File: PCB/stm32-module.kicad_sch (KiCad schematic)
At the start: 26 parts, among them J1 Conn_01x30_Socket, J2 Conn_01x30_Socket, J3 TYPE-C_16PIN_2MD__073_

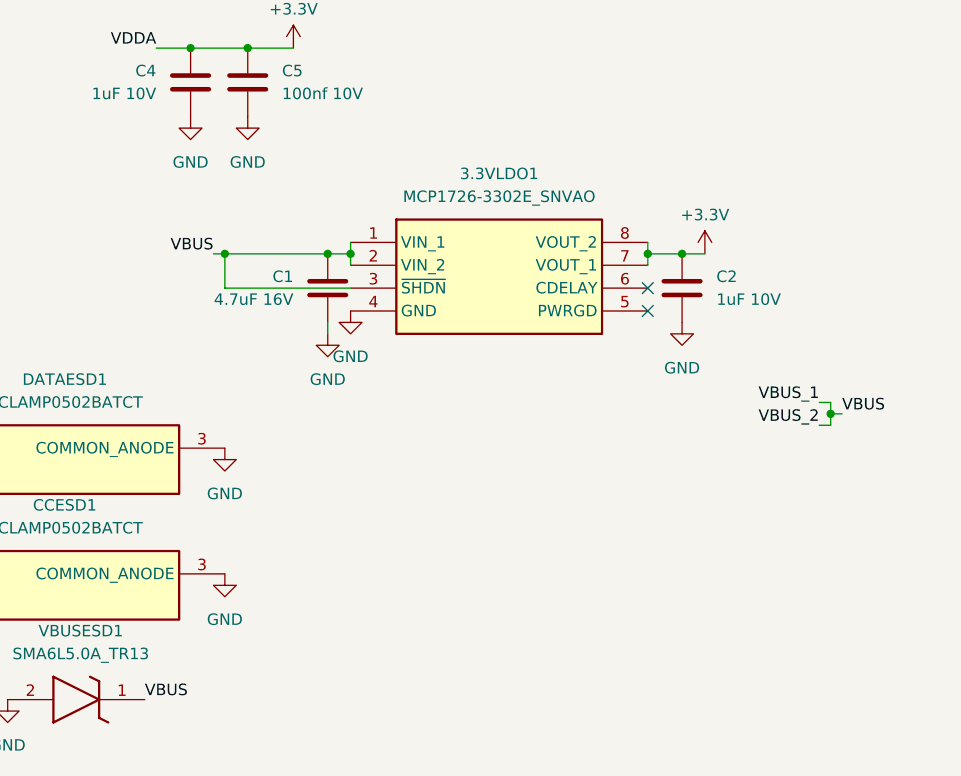
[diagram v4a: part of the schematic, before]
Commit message: Changed ldo due to availability
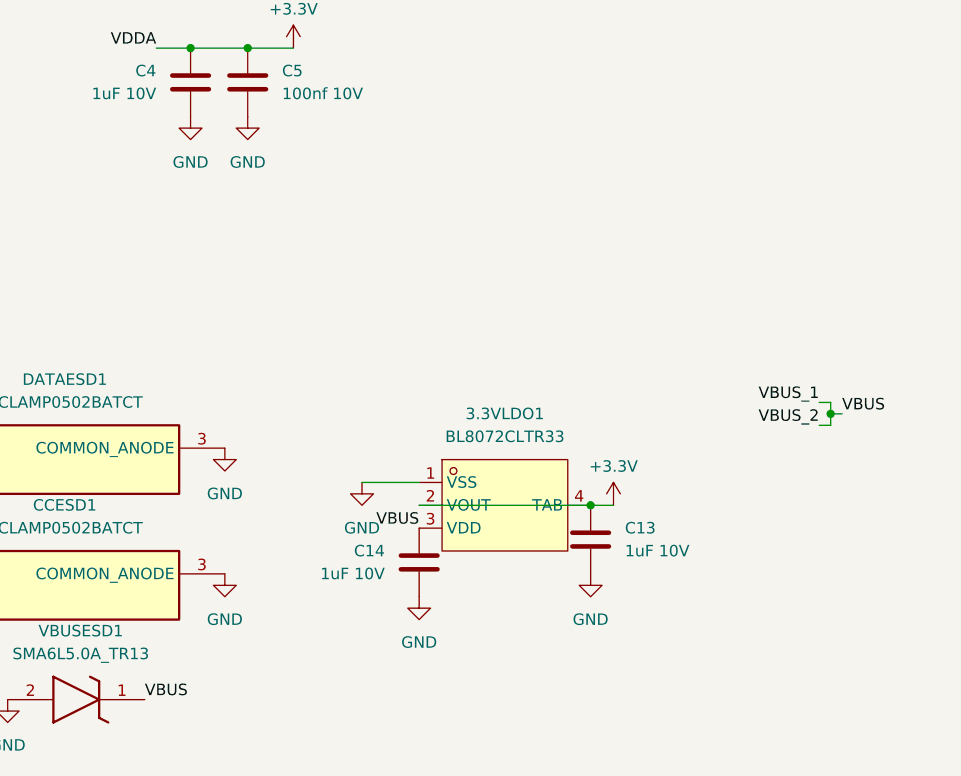
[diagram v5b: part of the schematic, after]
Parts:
- removed 3.3VLDO1: MCP1726-3302E_SNVAO, SamacSys_Parts:SOIC127P600X175-8N, symbol REQUIRED:MCP1726-3302E_SNVAO
- removed C1: 4.7uF 16V, Capacitor_SMD:C_0603_1608Metric_Pad1.08x0.95mm_HandSolder, symbol REQUIRED:C
- removed C2: 1uF 10V, Capacitor_SMD:C_0603_1608Metric_Pad1.08x0.95mm_HandSolder, symbol REQUIRED:C
- added 3.3VLDO1: BL8072CLTR33, easyeda2kicad:SOT-223-3_L6.5-W3.4-P2.30-LS7.0-BR, symbol easyeda2kicad:BL8072CLTR33
- added C13, C14: 1uF 10V, Capacitor_SMD:C_0603_1608Metric_Pad1.08x0.95mm_HandSolder, symbol REQUIRED:C
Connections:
- net +3.3V: now also 3.3VLDO1.2 (VOUT), 3.3VLDO1.4 (TAB), C13.1
- net GND: now also 3.3VLDO1.1 (VSS), C13.2, C14.2
- net VBUS: now also 3.3VLDO1.3 (VDD), C14.1
- no-connect marks 6 -> 4
